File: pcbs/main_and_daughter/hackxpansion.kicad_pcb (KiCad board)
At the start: 4 copper layers, 52 x 69 mm, 97 parts, among them CN1 533981471, CN2 533981471, CN3 533981471, CN4 533981471, IC1 ADS7128IRTET, J1 Conn_01x03_MountingPin, J2 USB_C_Receptacle_USB2.0_14P, Q1 BSS138, Q2 2N7002, SW1 SW_Push, SW2 SW_Push, SW3 SW_On_Off, U2 RP2354B, U5 SPX3819M5-L-3-3, U7 BQ24075RGT, U8 USBLC6-2SC6, Y1 ABM8-272-T3

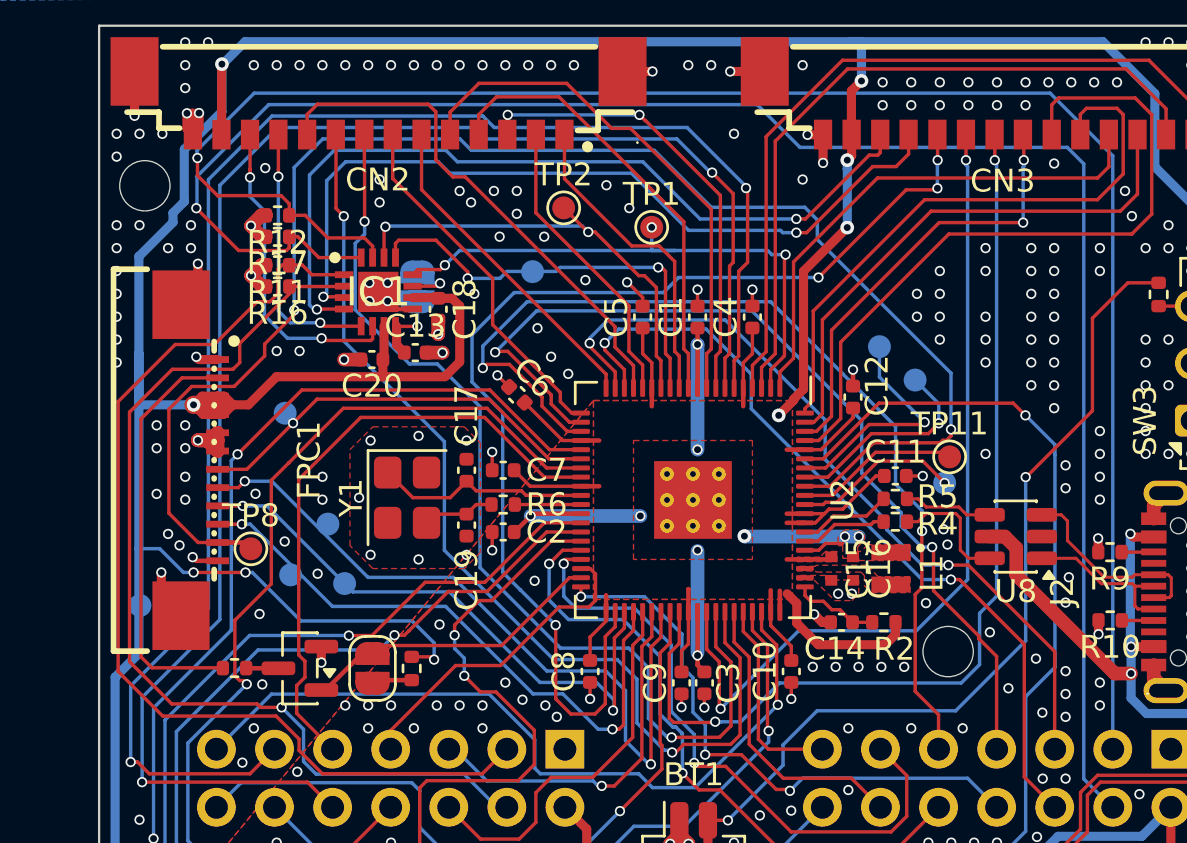
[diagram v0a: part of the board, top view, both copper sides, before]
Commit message: removed display brightness control, ran out of pin
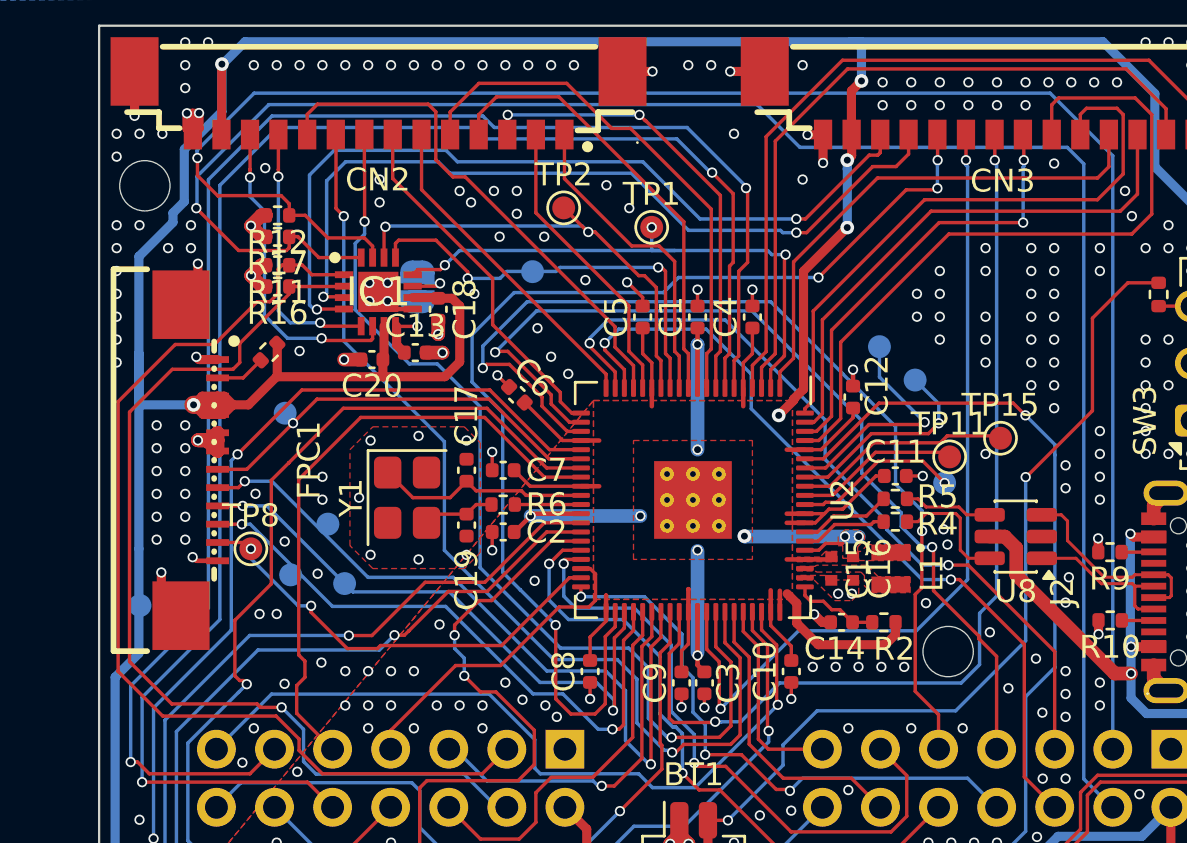
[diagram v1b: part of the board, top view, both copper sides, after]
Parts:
- removed JP3: SolderJumper_2_Open, Jumper:SolderJumper-2_P1.3mm_Open_RoundedPad1.0x1.5mm
- removed Q1: BSS138, Package_TO_SOT_SMD:SOT-23
- removed R7: 10, Resistor_SMD:R_0402_1005Metric
- added TP15: TestPoint, TestPoint:TestPoint_Pad_D1.0mm, F.Cu at (141.3, 75.9)
- moved R8 15.2 mm to (109.3, 72.2), turned to 45 degrees
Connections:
- R8 pad 1: Net-(JP3-A) -> Net-(FPC1-Pad2)
- U2 pad 39: /Main Board/Display/BACKLIGHT -> /Main Board/Display/RESET
- U2 pad 72: /Main Board/Display/RESET -> Net-(U2-QSPI_SD0)
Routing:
- net /Main Board/Display/RESET: track 66.7 -> 19.5 mm
- net Net-(FPC1-Pad2): track 18.3 -> 2.21 mm
- net /+3V3: track 301.3 -> 286.4 mm, vias 13 -> 10
- net /Main Board/Display/BACKLIGHT: track 13.4 -> 0.00 mm
- net Net-(U2-QSPI_SD0): track 0.00 -> 9.51 mm
- net Net-(JP3-A): track 1.77 -> 0.00 mm
- net Net-(Q1-D): track 1.41 -> 0.00 mm
- net /GND: track 65.1 -> 64.4 mm, vias 377 -> 384

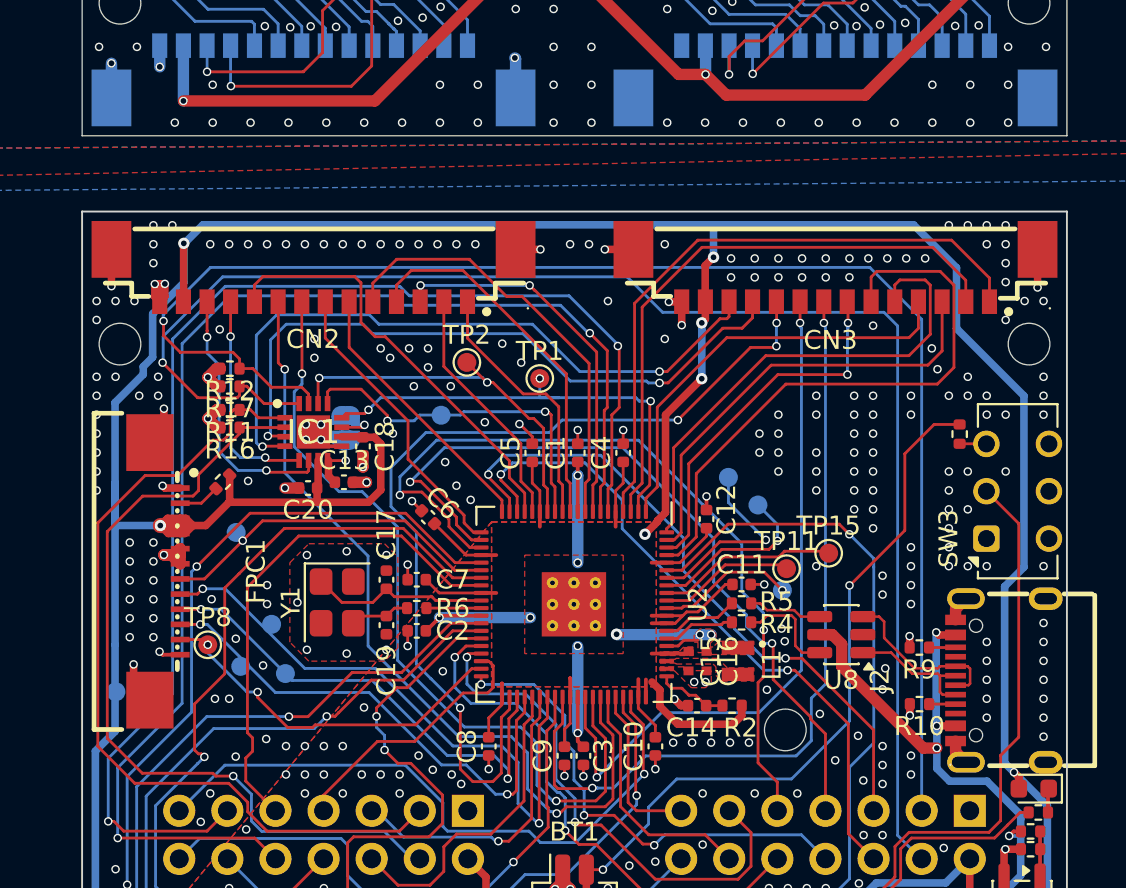
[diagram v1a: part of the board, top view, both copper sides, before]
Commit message: added back display brightness, removed adc allert on pcb
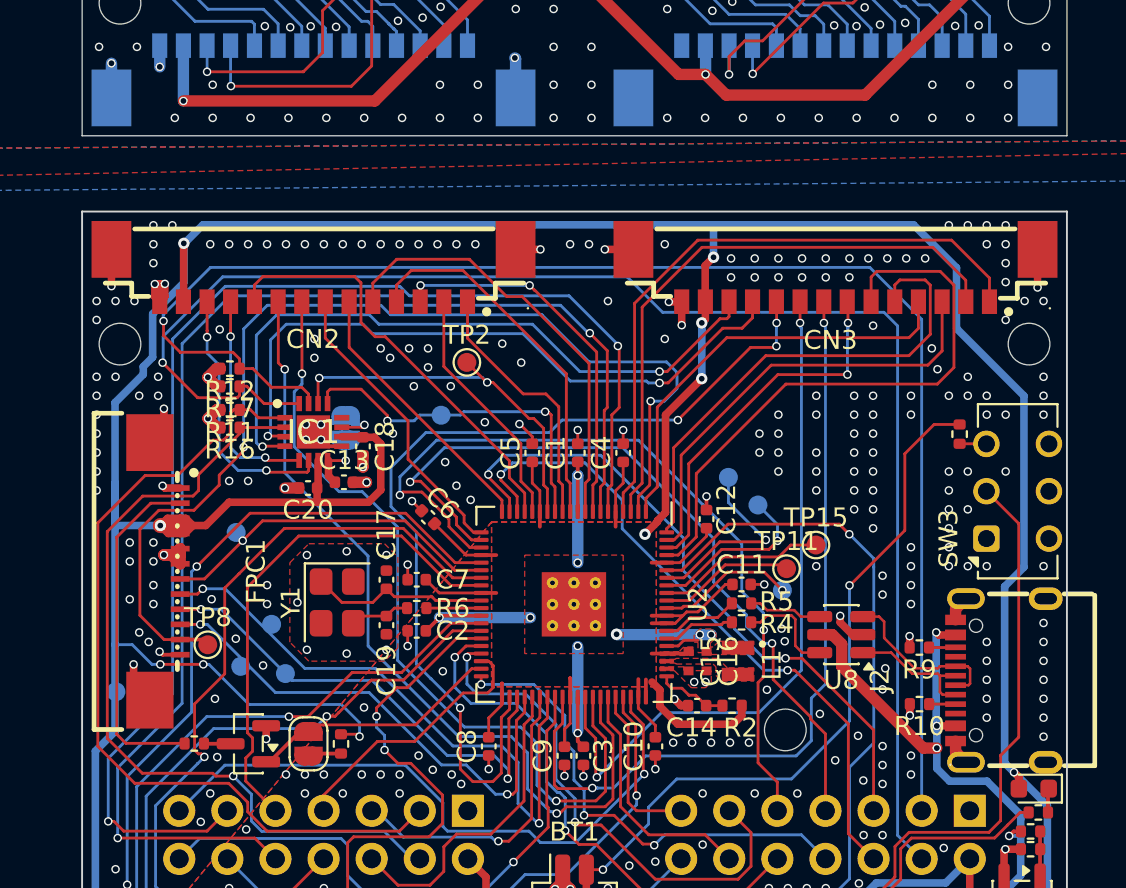
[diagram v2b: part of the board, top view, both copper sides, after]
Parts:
- removed TP1: TestPoint, TestPoint:TestPoint_Pad_D1.0mm
- added JP3: SolderJumper_2_Open, Jumper:SolderJumper-2_P1.3mm_Open_RoundedPad1.0x1.5mm, F.Cu at (113.8, 86.0)
- added Q1: BSS138, Package_TO_SOT_SMD:SOT-23, F.Cu at (110.7, 86.0)
- added R7: 10, Resistor_SMD:R_0402_1005Metric, F.Cu at (107.8, 86.0)
- moved R8 15.2 mm to (115.5, 86.0), turned to 90 degrees
- moved TP15 0.80 mm to (140.6, 75.5)
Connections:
- IC1 pad 12: /Main Board/ADC/ALERT -> unconnected-(IC1-ALERT-Pad12)
- R8 pad 1: Net-(FPC1-Pad2) -> Net-(JP3-A)
- U2 pad 2: /Main Board/ADC/ALERT -> /Main Board/Display/RESET
- U2 pad 39: /Main Board/Display/RESET -> /Main Board/Display/BACKLIGHT
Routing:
- net /Main Board/Display/RESET: track 19.5 -> 56.2 mm
- net /Main Board/ADC/ALERT: track 25.0 -> 0.00 mm, vias 3 -> 0
- net Net-(FPC1-Pad2): track 2.21 -> 18.3 mm
- net /+3V3: track 286.4 -> 301.3 mm, vias 10 -> 13
- net /Main Board/Display/BACKLIGHT: track 0.00 -> 13.4 mm
- net /GND: track 64.4 -> 66.9 mm, vias 384 -> 378
- net Net-(JP3-A): track 0.00 -> 1.77 mm
- net Net-(Q1-D): track 0.00 -> 1.41 mm
- net Net-(U2-QSPI_SD0): track 9.51 -> 8.93 mm

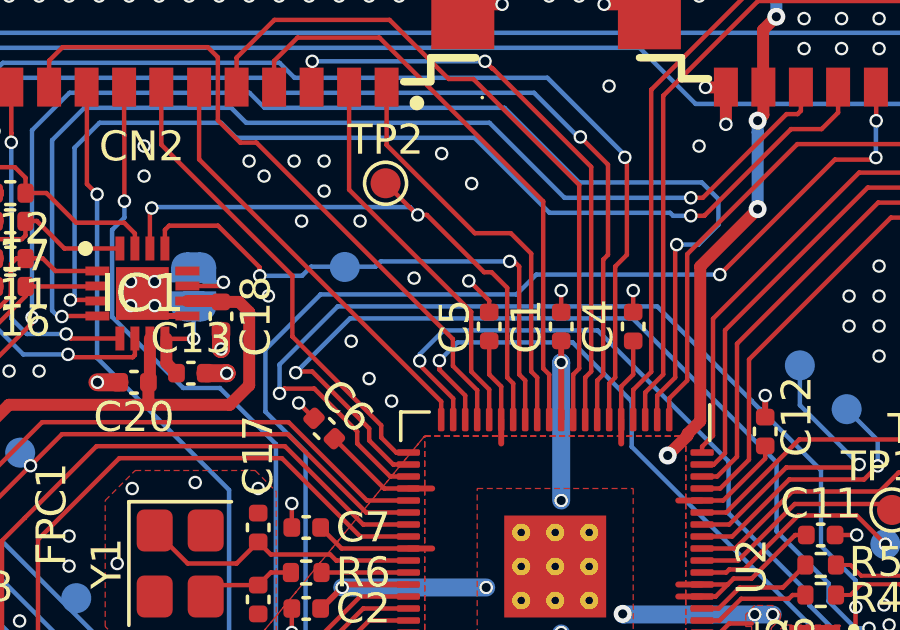
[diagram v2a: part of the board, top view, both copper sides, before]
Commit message: switched the two i2c pins on the rpi for the adc
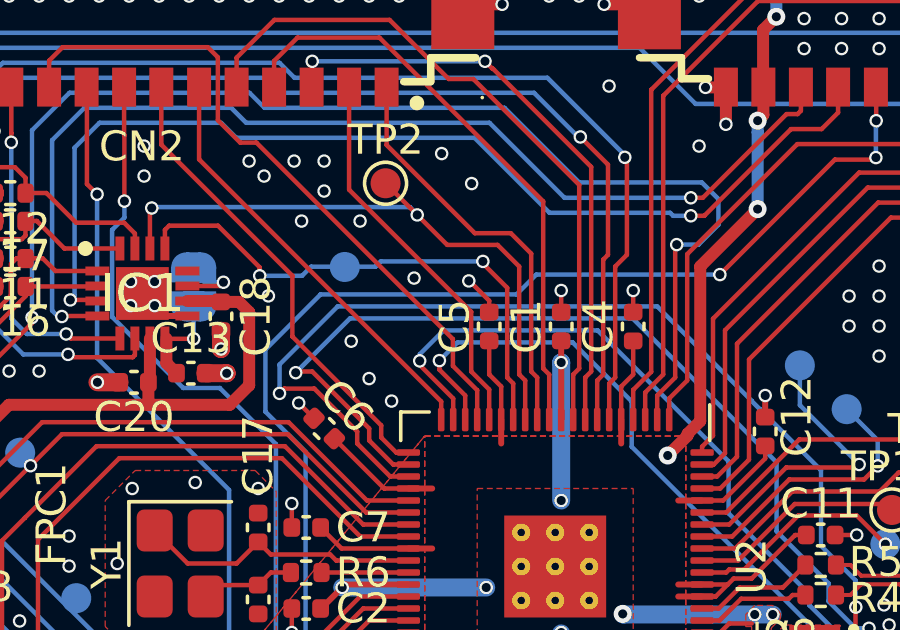
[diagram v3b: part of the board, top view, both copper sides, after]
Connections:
- U2 pad 13: /Main Board/ADC/SCL -> /Main Board/ADC/SDA
- U2 pad 14: /Main Board/ADC/SDA -> /Main Board/ADC/SCL
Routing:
- net /Main Board/ADC/SDA: track 20.3 -> 21.2 mm
- net /Main Board/ADC/SCL: track 18.8 -> 18.0 mm
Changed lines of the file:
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@@
 			(layers "F.Cu" "F.Mask" "F.Paste")
 			(roundrect_rratio 0.25)
-			(net "/Main Board/ADC/SCL")
+			(net "/Main Board/ADC/SDA")
 			(pinfunction "GPIO14_13")
 			(pintype "bidirectional")
@@
 			(layers "F.Cu" "F.Mask" "F.Paste")
 			(roundrect_rratio 0.25)
-			(net "/Main Board/ADC/SDA")
+			(net "/Main Board/ADC/SCL")
 			(pinfunction "GPIO15_14")
 			(pintype "bidirectional")
@@
 	)
 	(segment
-		(start 126.640003 68.64)
-		(end 126.470003 68.47)
+		(start 126.240001 69.350001)
+		(end 125.43 68.54)
 		(width 0.15)
 		(layer "F.Cu")
@@
 	)
 	(segment
-		(start 114.97 67.28)
-		(end 114.83 67.42)
+		(start 126.440002 73.743501)
+		(end 126.440002 72.540001)
 		(width 0.15)
 		(layer "F.Cu")
@@
 	)
 	(segment
-		(start 126.840001 73.743499)
-		(end 126.840002 72.440001)
+		(start 126.440002 72.540001)
+		(end 126.240001 72.34)
 		(width 0.15)
 		(layer "F.Cu")
@@
 	)
 	(segment
-		(start 126.840002 72.440001)
-		(end 126.640002 72.239999)
+		(start 126.240001 72.34)
+		(end 126.240001 69.350001)
 		(width 0.15)
 		(layer "F.Cu")
@@
 	)
 	(segment
-		(start 126.470003 68.47)
-		(end 126.32 68.47)
+		(start 114.97 67.28)
+		(end 114.83 67.42)
 		(width 0.15)
 		(layer "F.Cu")
@@
 	)
 	(segment
-		(start 126.640002 72.239999)
-		(end 126.640003 68.64)
+		(start 125.43 68.54)
+		(end 125.43 68.47)
 		(width 0.15)
 		(layer "F.Cu")
@@
 	)
 	(via
-		(at 126.32 68.47)
+		(at 125.43 68.47)
 		(size 0.45)
 		(drill 0.3)
@@
 	(segment
 		(start 122.026444 68.47)
-		(end 126.32 68.47)
+		(end 125.43 68.47)
 		(width 0.15)
 		(layer "B.Cu")
@@
 	)
 	(segment
-		(start 123.56 66.92)
-		(end 125.47 68.83)
-		(width 0.15)
-		(layer "F.Cu")
-		(net "/Main Board/ADC/SDA")
-	)
-	(segment
-		(start 123.26 66.92)
-		(end 123.240032 66.92)
-		(width 0.15)
-		(layer "F.Cu")
-		(net "/Main Board/ADC/SDA")
-	)
-	(segment
-		(start 125.47 68.83)
-		(end 125.72 68.83)
+		(start 126.840001 73.743499)
+		(end 126.840002 72.440001)
 		(width 0.15)
 		(layer "F.Cu")
@@
 	)
 	(segment
-		(start 123.26 66.92)
-		(end 123.56 66.92)
+		(start 126.640003 68.64)
+		(end 125.920003 67.92)
 		(width 0.15)
 		(layer "F.Cu")
@@
 	)
 	(segment
-		(start 125.72 68.83)
-		(end 126.240001 69.350001)
+		(start 124.240032 67.92)
+		(end 123.240032 66.92)
 		(width 0.15)
 		(layer "F.Cu")
@@
 	)
 	(segment
-		(start 126.240001 72.34)
-		(end 126.440002 72.540001)
+		(start 125.920003 67.92)
+		(end 124.240032 67.92)
 		(width 0.15)
 		(layer "F.Cu")
@@
 	)
 	(segment
-		(start 126.440002 72.540001)
-		(end 126.440002 73.743501)
+		(start 126.640002 72.239999)
+		(end 126.640003 68.64)
 		(width 0.15)
 		(layer "F.Cu")
@@
 	)
 	(segment
-		(start 114.39 66.69)
-		(end 114.33 66.75)
+		(start 126.840002 72.440001)
+		(end 126.640002 72.239999)
 		(width 0.15)
 		(layer "F.Cu")
@@
 	)
 	(segment
-		(start 126.240001 69.350001)
-		(end 126.240001 72.34)
+		(start 114.39 66.69)
+		(end 114.33 66.75)
 		(width 0.15)
 		(layer "F.Cu")
@@
 	)
 	(via
-		(at 123.26 66.92)
+		(at 123.240032 66.92)
 		(size 0.45)
 		(drill 0.3)
@@
 	)
 	(segment
+		(start 138.65614 76.139999)
+		(end 139.286139 75.51)
+		(width 0.15)
+		(layer "F.Cu")
+		(net "Net-(U2-QSPI_SD0)")
+	)
+	(segment
+		(start 135.740002 76.139999)
+		(end 138.65614 76.139999)
+		(width 0.15)
+		(layer "F.Cu")
+		(net "Net-(U2-QSPI_SD0)")
+	)
+	(segment
+		(start 133.840001 78.04)
+		(end 135.740002 76.139999)
+		(width 0.15)
+		(layer "F.Cu")
+		(net "Net-(U2-QSPI_SD0)")
+	)
+	(segment
+		(start 139.286139 75.51)
+		(end 140.62 75.51)
+		(width 0.15)
+		(layer "F.Cu")
+		(net "Net-(U2-QSPI_SD0)")
+	)
+	(segment
+		(start 132.736503 78.04)
+		(end 133.840001 78.04)
+		(width 0.15)
+		(layer "F.Cu")
+		(net "Net-(U2-QSPI_SD0)")
+	)
+	(segment
 		(start 133.545003 83.07)
 		(end 133.915002 83.439999)
@@
 		(net "Net-(U2-QSPI_SD1)")
 	)
-	(segment
-		(start 138.65614 76.139999)
-		(end 139.286139 75.51)
-		(width 0.15)
-		(layer "F.Cu")
-		(net "Net-(U2-QSPI_SD0)")
-	)
-	(segment
-		(start 135.740002 76.139999)
-		(end 138.65614 76.139999)
-		(width 0.15)
-		(layer "F.Cu")
-		(net "Net-(U2-QSPI_SD0)")
-	)
-	(segment
-		(start 133.840001 78.04)
-		(end 135.740002 76.139999)
-		(width 0.15)
-		(layer "F.Cu")
-		(net "Net-(U2-QSPI_SD0)")
-	)
-	(segment
-		(start 139.286139 75.51)
-		(end 140.62 75.51)
-		(width 0.15)
-		(layer "F.Cu")
-		(net "Net-(U2-QSPI_SD0)")
-	)
-	(segment
-		(start 132.736503 78.04)
-		(end 133.840001 78.04)
-		(width 0.15)
-		(layer "F.Cu")
-		(net "Net-(U2-QSPI_SD0)")
-	)
 	(zone
